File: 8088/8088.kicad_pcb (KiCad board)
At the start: 2 copper layers, 157.5 x 93.5 mm, 194 parts, among them P10 CONN_01X15, P11 CONN_01X05, P12 CONN_01X05, P13 CONN_01X08, P14 CONN_01X08, P9 CONN_01X06, U1 8284, U10 2114, U11 ULN2803ADWR, U12 74LS14, U13 ULN2803ADWR, U14 ULN2803ADWR, U15 ULN2803ADWR, U16 LM1084IT-5.0/NOPB, U2 8088, U3 8755A, U3PA U3PA, U3PB U3PB, U4 8155, U4PA U4PA, U4PB U4PB, U4PC U4PC, U5 8251A, U6 74LS32, U7 74LS138, U8 8282, U9 2114, Y1 12MHz

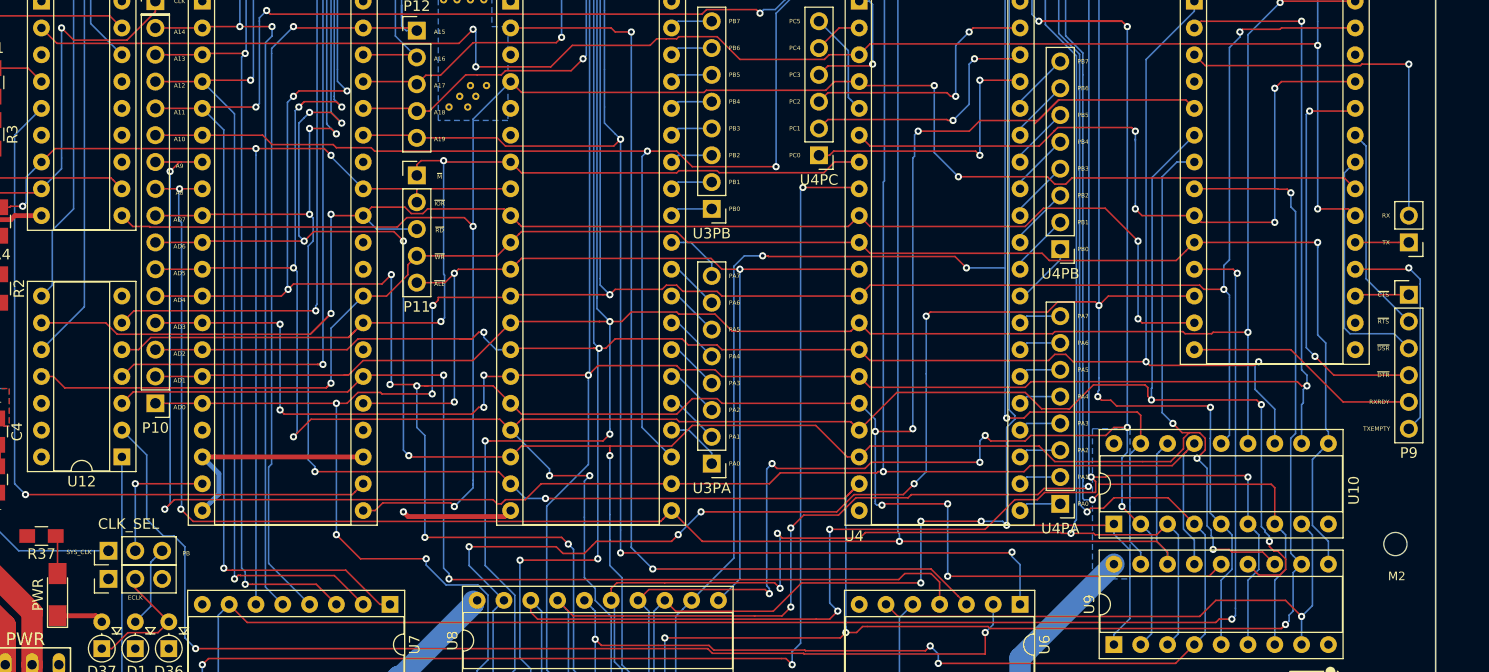
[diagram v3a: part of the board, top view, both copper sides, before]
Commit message: Fixed some silkscreen issues
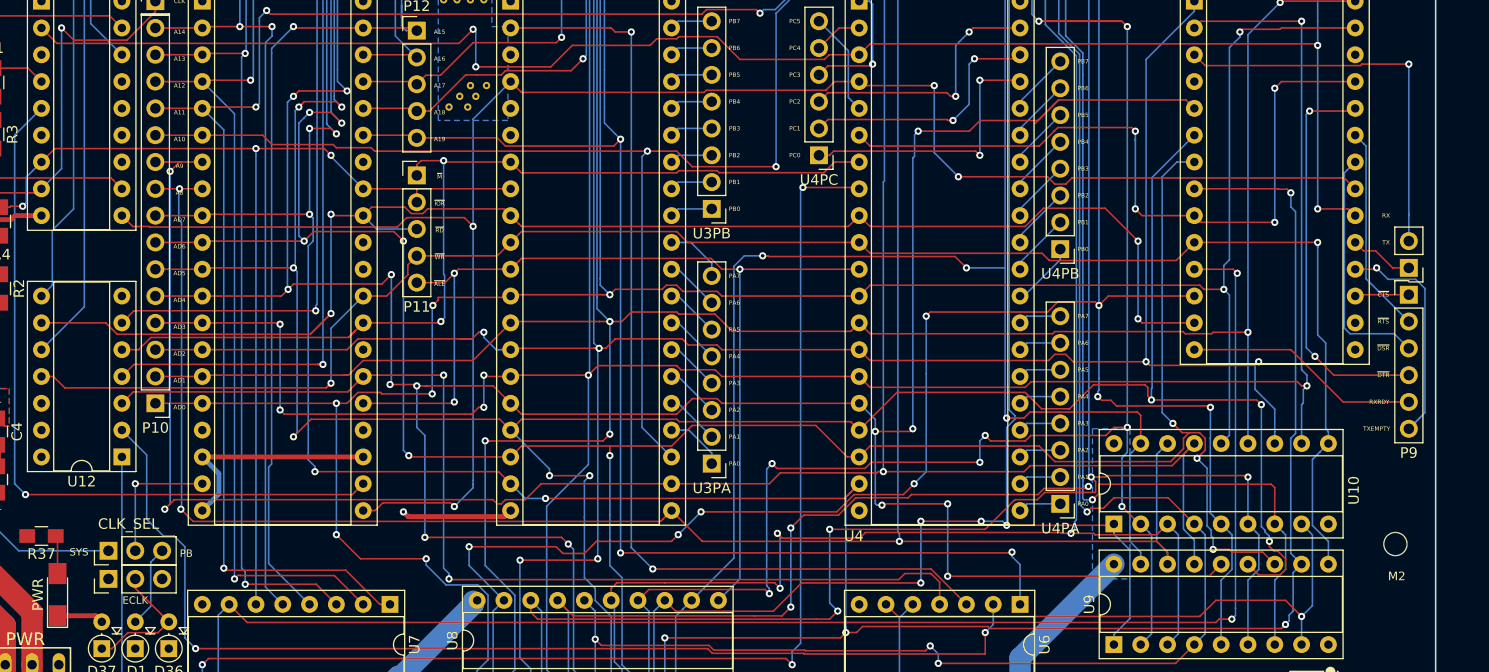
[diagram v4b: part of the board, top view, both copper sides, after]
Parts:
- moved RX/TX 2.41 mm to (228.6, 89.4)
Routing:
- net Net-(P4-Pad2): track 35.2 -> 37.7 mm
- net /TXEMP: track 21.4 -> 23.1 mm
- net Net-(P4-Pad1): track 5.08 -> 6.08 mm
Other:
- board text added: "SYS"
- board text removed: "SYS_CLK"
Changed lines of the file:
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@@
     (thickness 1.6)
     (drawings 93)
-    (tracks 2160)
+    (tracks 2167)
     (zones 0)
     (modules 194)
@@
   )
   (module Pin_Headers:Pin_Header_Straight_1x02_Pitch2.54mm (layer F.Cu)
-    (at 228.6 86.995 180)
+    (at 228.6 89.408 180)
     (descr "Through hole straight pin header, 1x02, 2.54mm pitch, single row")
     (tags "Through hole pin header THT 1x02 2.54mm single row")
@@
     (effects (font (size 0.6 0.6) (thickness 0.1)))
   )
-  (gr_text ECLK (at 107.95 120.65) (layer F.SilkS)
-    (effects (font (size 0.4064 0.4064) (thickness 0.0762)))
+  (gr_text ECLK (at 107.95 120.904) (layer F.SilkS)
+    (effects (font (size 0.7 0.7) (thickness 0.0762)))
   )
   (gr_text PB (at 112.776 116.459) (layer F.SilkS)
-    (effects (font (size 0.4064 0.4064) (thickness 0.0762)))
+    (effects (font (size 0.7 0.7) (thickness 0.0762)))
   )
-  (gr_text SYS_CLK (at 102.616 116.332) (layer F.SilkS)
-    (effects (font (size 0.4064 0.4064) (thickness 0.0762)))
+  (gr_text SYS (at 102.616 116.332) (layer F.SilkS)
+    (effects (font (size 0.7 0.7) (thickness 0.0762)))
   )
   (gr_text A7 (at 160.274 132.334 90) (layer F.SilkS)
@@
   )
   (gr_line (start 73.66 134.62) (end 231.14 134.62) (layer Edge.Cuts) (width 0.15))
-  (dimension 154.94 (width 0.0762) (layer Eco2.User)
-    (gr_text "154.940 mm" (at 153.67 31.8262) (layer Eco2.User)
+  (dimension 157.480051 (width 0.0762) (layer Eco2.User)
+    (gr_text "157.480 mm" (at 152.407619 31.762703 359.9537937) (layer Eco2.User)
       (effects (font (size 0.8128 0.8128) (thickness 0.0762)))
     )
-    (feature1 (pts (xy 231.14 41.275) (xy 231.14 31.2674)))
-    (feature2 (pts (xy 76.2 41.275) (xy 76.2 31.2674)))
-    (crossbar (pts (xy 76.2 32.385) (xy 231.14 32.385)))
-    (arrow1a (pts (xy 231.14 32.385) (xy 230.013496 32.971421)))
-    (arrow1b (pts (xy 231.14 32.385) (xy 230.013496 31.798579)))
-    (arrow2a (pts (xy 76.2 32.385) (xy 77.326504 32.971421)))
-    (arrow2b (pts (xy 76.2 32.385) (xy 77.326504 31.798579)))
+    (feature1 (pts (xy 231.14 41.275) (xy 231.14807 31.267403)))
+    (feature2 (pts (xy 73.66 41.148) (xy 73.66807 31.140403)))
+    (crossbar (pts (xy 73.667169 32.258003) (xy 231.147169 32.385003)))
+    (arrow1a (pts (xy 231.147169 32.385003) (xy 230.020193 32.970515)))
+    (arrow1b (pts (xy 231.147169 32.385003) (xy 230.021139 31.797674)))
+    (arrow2a (pts (xy 73.667169 32.258003) (xy 74.793199 32.845332)))
+    (arrow2b (pts (xy 73.667169 32.258003) (xy 74.794145 31.672491)))
   )
   (gr_line (start 73.66 134.62) (end 73.66 41.148) (layer Edge.Cuts) (width 0.15))
@@
   (segment (start 119.40806 48.641108) (end 119.323062 48.641108) (width 0.25) (layer B.Cu) (net 0))
   (segment (start 138.429892 48.641108) (end 138.394168 48.641108) (width 0.25) (layer B.Cu) (net 0))
+  (segment (start 91.948 90.275) (end 90.563 91.66) (width 0.1524) (layer F.Cu) (net 1))
+  (segment (start 90.563 91.66) (end 90.17 91.66) (width 0.1524) (layer F.Cu) (net 1))
   (segment (start 95.25 90.01) (end 92.088 90.01) (width 0.1524) (layer F.Cu) (net 1))
   (segment (start 92.088 90.01) (end 91.948 90.15) (width 0.1524) (layer F.Cu) (net 1))
   (segment (start 91.948 90.15) (end 91.948 90.275) (width 0.1524) (layer F.Cu) (net 1))
-  (segment (start 91.948 90.275) (end 90.563 91.66) (width 0.1524) (layer F.Cu) (net 1))
-  (segment (start 90.563 91.66) (end 90.17 91.66) (width 0.1524) (layer F.Cu) (net 1))
+  (segment (start 91.46 87.65) (end 90.17 86.36) (width 0.4572) (layer F.Cu) (net 2))
+  (segment (start 91.948 87.65) (end 91.46 87.65) (width 0.4572) (layer F.Cu) (net 2))
   (segment (start 133.35 112.522) (end 133.794391 112.966391) (width 0.4572) (layer F.Cu) (net 2))
   (segment (start 133.794391 112.966391) (end 142.938609 112.966391) (width 0.4572) (layer F.Cu) (net 2))
@@
   (segment (start 96.159802 84.836) (end 93.472 84.836) (width 0.4572) (layer F.Cu) (net 2))
   (via (at 93.472 84.836) (size 0.6858) (drill 0.3302) (layers F.Cu B.Cu) (net 2))
-  (segment (start 91.948 87.65) (end 91.46 87.65) (width 0.4572) (layer F.Cu) (net 2))
-  (segment (start 91.46 87.65) (end 90.17 86.36) (width 0.4572) (layer F.Cu) (net 2))
   (segment (start 91.948 72.918) (end 91.948 72.898) (width 0.4572) (layer F.Cu) (net 2))
   (segment (start 91.948 72.898) (end 90.17 71.12) (width 0.4572) (layer F.Cu) (net 2))
@@
   (segment (start 162.56 66.04) (end 159.385 66.04) (width 0.1524) (layer B.Cu) (net 93))
   (segment (start 159.385 66.04) (end 158.75 66.675) (width 0.1524) (layer B.Cu) (net 93))
-  (segment (start 228.6 86.995) (end 227.5976 86.995) (width 0.1524) (layer F.Cu) (net 94))
-  (segment (start 227.5976 86.995) (end 223.52 86.995) (width 0.1524) (layer F.Cu) (net 94))
+  (segment (start 227.076 89.408) (end 228.6 89.408) (width 0.1524) (layer F.Cu) (net 94))
+  (segment (start 225.462999 87.794999) (end 227.076 89.408) (width 0.1524) (layer F.Cu) (net 94))
+  (segment (start 223.52 86.995) (end 224.319999 87.794999) (width 0.1524) (layer F.Cu) (net 94))
+  (segment (start 224.319999 87.794999) (end 225.462999 87.794999) (width 0.1524) (layer F.Cu) (net 94))
+  (segment (start 228.6 84.455) (end 228.6 84.328) (width 0.1524) (layer B.Cu) (net 95))
+  (segment (start 228.6 84.328) (end 228.6 70.104) (width 0.1524) (layer B.Cu) (net 95))
+  (segment (start 228.6 86.868) (end 228.6 84.328) (width 0.1524) (layer B.Cu) (net 95))
   (segment (start 228.6 70.104) (end 224.15333 70.104) (width 0.1524) (layer F.Cu) (net 95))
   (segment (start 224.15333 70.104) (end 224.013729 70.243601) (width 0.1524) (layer F.Cu) (net 95))
@@
   (segment (start 209.308601 70.243601) (end 209.079999 70.014999) (width 0.1524) (layer F.Cu) (net 95))
   (segment (start 209.079999 70.014999) (end 208.28 69.215) (width 0.1524) (layer F.Cu) (net 95))
-  (segment (start 228.6 84.455) (end 228.6 70.104) (width 0.1524) (layer B.Cu) (net 95))
   (via (at 228.6 70.104) (size 0.6858) (drill 0.3302) (layers F.Cu B.Cu) (net 95))
   (segment (start 187.96 71.628) (end 191.643 71.628) (width 0.1524) (layer F.Cu) (net 96))
@@
   (segment (start 217.424 97.155) (end 209.41137 97.155) (width 0.1524) (layer F.Cu) (net 177))
   (segment (start 209.41137 97.155) (end 208.28 97.155) (width 0.1524) (layer F.Cu) (net 177))
-  (segment (start 229.678601 103.569399) (end 229.678601 90.932) (width 0.1524) (layer B.Cu) (net 178))
-  (segment (start 228.6 89.408) (end 229.678601 90.486601) (width 0.1524) (layer B.Cu) (net 178))
-  (segment (start 229.678601 90.486601) (end 229.678601 90.932) (width 0.1524) (layer B.Cu) (net 178))
-  (segment (start 223.52 89.535) (end 228.473 89.535) (width 0.1524) (layer F.Cu) (net 178))
-  (segment (start 228.473 89.535) (end 228.6 89.408) (width 0.1524) (layer F.Cu) (net 178))
+  (segment (start 229.616 103.632) (end 228.6 104.648) (width 0.1524) (layer B.Cu) (net 178))
+  (segment (start 230.124 103.124) (end 229.616 103.632) (width 0.1524) (layer B.Cu) (net 178))
+  (segment (start 230.124 91.360518) (end 230.124 103.124) (width 0.1524) (layer B.Cu) (net 178))
+  (segment (start 225.552 89.408) (end 226.630601 90.486601) (width 0.1524) (layer B.Cu) (net 178))
+  (segment (start 226.630601 90.486601) (end 229.250083 90.486601) (width 0.1524) (layer B.Cu) (net 178))
+  (segment (start 229.250083 90.486601) (end 230.124 91.360518) (width 0.1524) (layer B.Cu) (net 178))
+  (segment (start 229.678601 103.569399) (end 228.6 104.648) (width 0.1524) (layer B.Cu) (net 178))
+  (segment (start 223.52 89.535) (end 225.425 89.535) (width 0.1524) (layer F.Cu) (net 178))
+  (segment (start 225.425 89.535) (end 225.552 89.408) (width 0.1524) (layer F.Cu) (net 178))
+  (via (at 225.552 89.408) (size 0.6858) (drill 0.3302) (layers F.Cu B.Cu) (net 178))
   (segment (start 223.647 89.408) (end 223.52 89.535) (width 0.1524) (layer F.Cu) (net 178))
-  (segment (start 228.6 104.648) (end 229.678601 103.569399) (width 0.1524) (layer B.Cu) (net 178))
-  (via (at 228.6 89.408) (size 0.6858) (drill 0.3302) (layers F.Cu B.Cu) (net 178))
+  (segment (start 95.25 83.66) (end 96.0524 83.66) (width 0.1524) (layer F.Cu) (net 179))
+  (segment (start 96.0524 83.66) (end 96.1464 83.566) (width 0.1524) (layer F.Cu) (net 179))
+  (segment (start 96.1464 83.566) (end 97.282 83.566) (width 0.1524) (layer F.Cu) (net 179))
   (segment (start 129.54 81.915) (end 134.62 81.915) (width 0.1524) (layer F.Cu) (net 179))
   (segment (start 134.62 81.915) (end 143.51 81.915) (width 0.1524) (layer F.Cu) (net 179))
@@
   (segment (start 97.624899 80.810101) (end 98.260001 80.174999) (width 0.1524) (layer B.Cu) (net 179))
   (segment (start 98.260001 80.174999) (end 99.06 79.375) (width 0.1524) (layer B.Cu) (net 179))
-  (segment (start 95.25 83.66) (end 96.0524 83.66) (width 0.1524) (layer F.Cu) (net 179))
-  (segment (start 96.0524 83.66) (end 96.1464 83.566) (width 0.1524) (layer F.Cu) (net 179))
-  (segment (start 96.1464 83.566) (end 97.282 83.566) (width 0.1524) (layer F.Cu) (net 179))
   (via (at 97.282 83.566) (size 0.6858) (drill 0.3302) (layers F.Cu B.Cu) (net 179))
   (segment (start 99.06 79.375) (end 100.33 78.105) (width 0.1524) (layer F.Cu) (net 179))

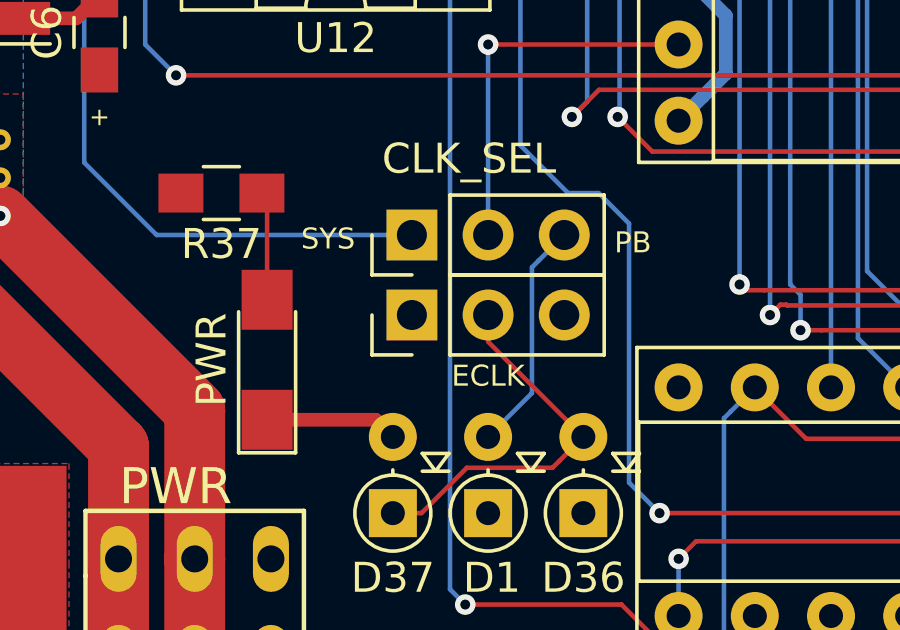
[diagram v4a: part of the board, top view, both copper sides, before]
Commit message: Fixed issue with ECLK
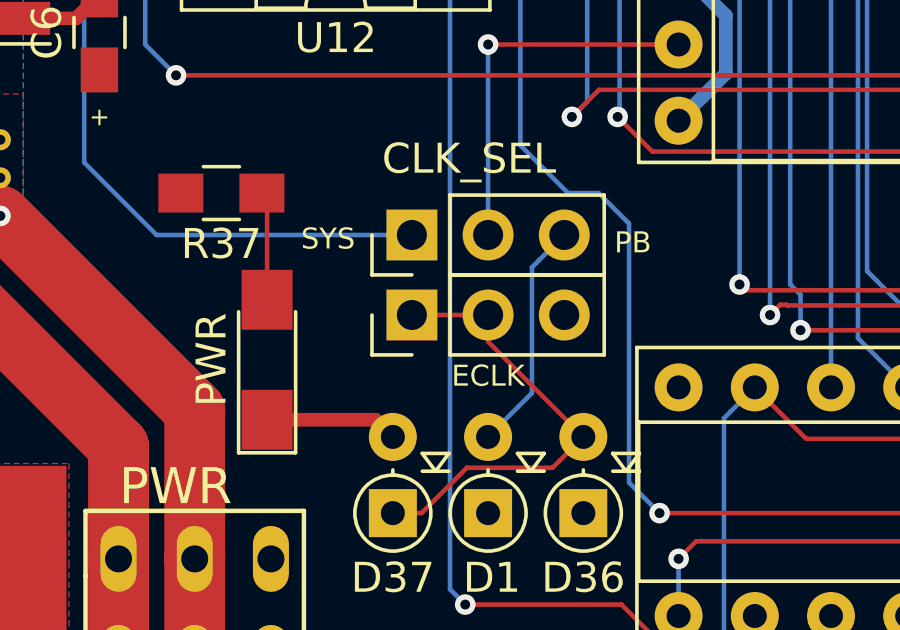
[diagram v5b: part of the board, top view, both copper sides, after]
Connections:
- JP2 pad 1: GND -> /ECLK
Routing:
- net /ECLK: track 12.9 -> 15.4 mm
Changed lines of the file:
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@@
     (thickness 1.6)
     (drawings 93)
-    (tracks 2167)
+    (tracks 2168)
     (zones 0)
     (modules 194)
@@
     )
     (pad 1 thru_hole rect (at 0 0 90) (size 1.7 1.7) (drill 1) (layers *.Cu *.Mask)
-      (net 2 GND))
+      (net 172 /ECLK))
     (pad 2 thru_hole oval (at 0 2.54 90) (size 1.7 1.7) (drill 1) (layers *.Cu *.Mask)
       (net 172 /ECLK))
@@
   (segment (start 106.68 94.615) (end 107.823 93.472) (width 0.1524) (layer F.Cu) (net 171))
   (via (at 125.0442 93.472) (size 0.6858) (drill 0.3302) (layers F.Cu B.Cu) (net 171))
+  (segment (start 105.41 118.872) (end 107.95 118.872) (width 0.1524) (layer F.Cu) (net 172))
   (segment (start 111.125 122.936) (end 107.95 119.761) (width 0.1524) (layer F.Cu) (net 172))
   (segment (start 107.95 119.761) (end 107.95 118.872) (width 0.1524) (layer F.Cu) (net 172))
